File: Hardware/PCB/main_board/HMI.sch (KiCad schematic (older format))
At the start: 4 parts

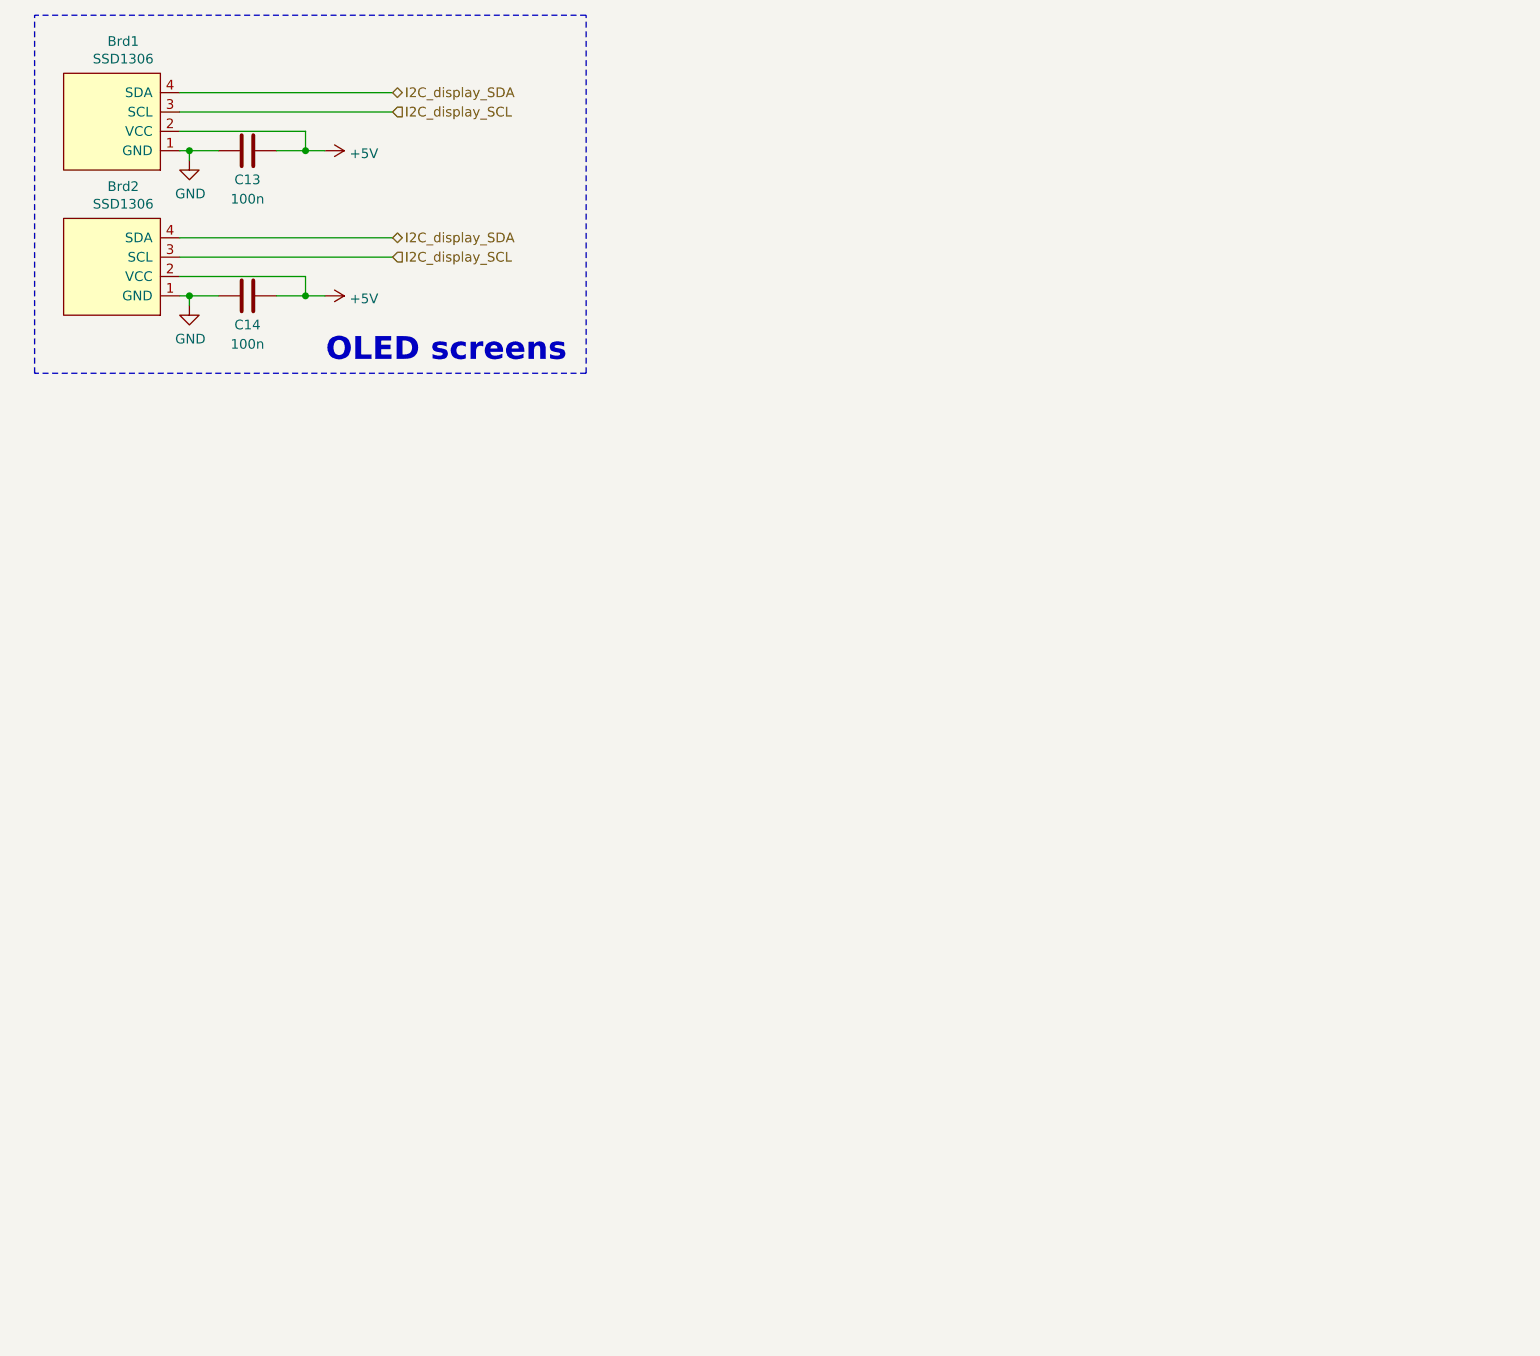
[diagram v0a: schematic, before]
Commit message: Add HMI buttons and pots to PCB
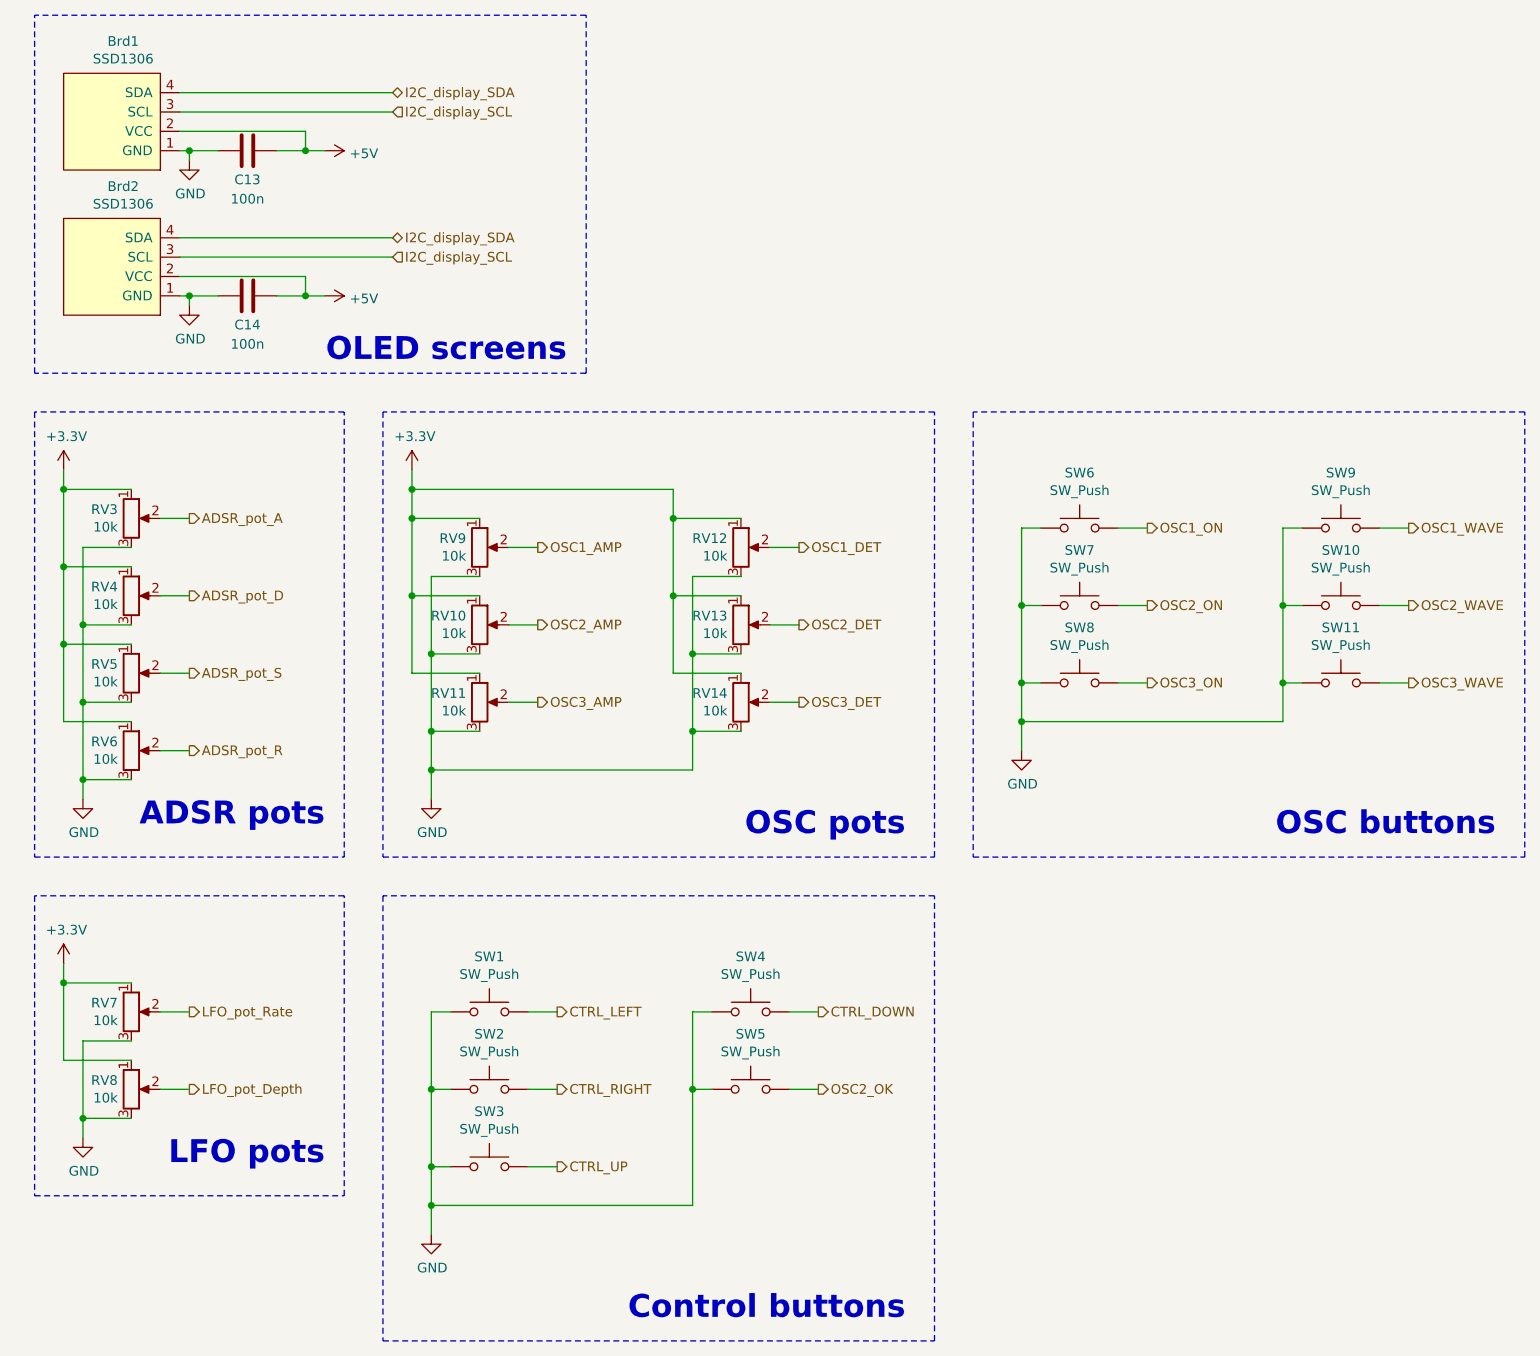
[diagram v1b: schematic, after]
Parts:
- added RV10, RV11, RV12, RV13, RV14, RV3, RV4, RV5, RV6, RV7, RV8, RV9: 10k, Potentiometer_THT:Potentiometer_Alps_RK09K_Single_Vertical, symbol Device:R_POT
- added SW1, SW10, SW11, SW2, SW3, SW4, SW5, SW6, SW7, SW8, SW9: SW_Push, Button_Switch_THT:SW_PUSH_6mm_H13mm, symbol Switch:SW_Push
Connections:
- net GND: now also RV10.3, RV11.3, RV12.3, RV13.3, RV14.3, RV3.3, RV4.3, RV5.3, RV6.3, RV7.3, RV8.3, RV9.3, SW1.1, SW10.1, SW11.1, SW2.1, SW3.1, SW4.1, SW5.1, SW6.1, SW7.1, SW8.1, SW9.1
- new net +3V3: RV10.1, RV11.1, RV12.1, RV13.1, RV14.1, RV3.1, RV4.1, RV5.1, RV6.1, RV7.1, RV8.1, RV9.1
- new net ADSR_pot_A: RV3.2
- new net ADSR_pot_D: RV4.2
- new net ADSR_pot_R: RV6.2
- new net ADSR_pot_S: RV5.2
- new net CTRL_DOWN: SW4.2
- new net CTRL_LEFT: SW1.2
- new net CTRL_RIGHT: SW2.2
- new net CTRL_UP: SW3.2
- new net LFO_pot_Depth: RV8.2
- new net LFO_pot_Rate: RV7.2
- new net OSC1_AMP: RV9.2
- new net OSC1_DET: RV12.2
- new net OSC1_ON: SW6.2
- new net OSC1_WAVE: SW9.2
- new net OSC2_AMP: RV10.2
- new net OSC2_DET: RV13.2
- new net OSC2_OK: SW5.2
- new net OSC2_ON: SW7.2
- new net OSC2_WAVE: SW10.2
- new net OSC3_AMP: RV11.2
- new net OSC3_DET: RV14.2
- new net OSC3_ON: SW8.2
- new net OSC3_WAVE: SW11.2
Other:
- note added: "ADSR pots"
- note added: "Control buttons"
- note added: "LFO pots"
- note added: "OSC buttons"
- note added: "OSC pots"

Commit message: Place HMI
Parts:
- renumbered RV3 to RV_ADSR_A1, RV4 to RV_ADSR_D1, RV6 to RV_ADSR_R1, RV5 to RV_ADSR_S1, RV8 to RV_LFO_DEPTH1, RV7 to RV_LFO_RATE1, RV9 to RV_OSC1_AMP1, RV12 to RV_OSC1_DET1, RV10 to RV_OSC2_AMP1, RV13 to RV_OSC2_DET1, RV11 to RV_OSC3_AMP1, RV14 to RV_OSC3_DET1, SW4 to SW_CTRL_DOWN1, SW1 to SW_CTRL_LEFT1, SW5 to SW_CTRL_OK1, SW2 to SW_CTRL_RIGHT1, SW3 to SW_CTRL_UP1, SW6 to SW_OSC1_ON1, SW9 to SW_OSC1_WAVE1, SW7 to SW_OSC2_ON1, SW10 to SW_OSC2_WAVE1, SW8 to SW_OSC3_ON1, SW11 to SW_OSC3_WAVE1
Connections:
- net LFO_pot_Depth renamed LFO_pot_DEPTH
- net LFO_pot_Rate renamed LFO_pot_RATE
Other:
- moved on the sheet: RV_LFO_DEPTH1, RV_LFO_RATE1, RV_OSC1_AMP1, RV_OSC1_DET1, RV_OSC2_AMP1, RV_OSC2_DET1, RV_OSC3_AMP1, RV_OSC3_DET1

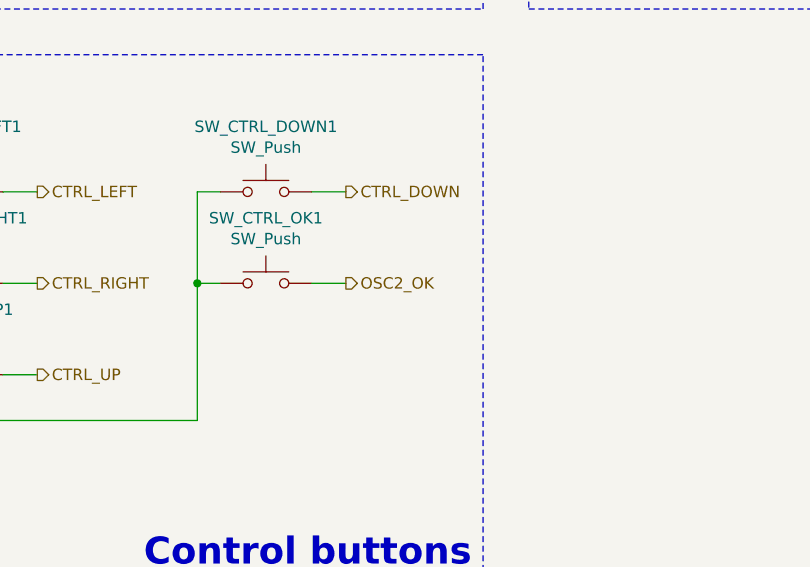
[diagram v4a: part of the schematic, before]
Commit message: Label GPIO, create HMI files
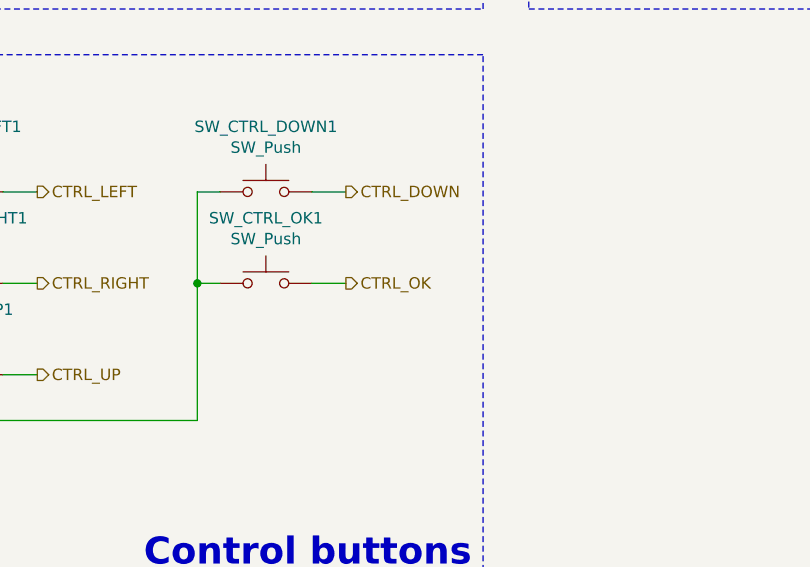
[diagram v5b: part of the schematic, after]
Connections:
- net OSC2_OK renamed CTRL_OK
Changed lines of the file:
@@
 	4600 6300 4750 6300
 Text HLabel 4750 6300 2    50   Output ~ 0
-OSC2_OK
+CTRL_OK
 Wire Wire Line
 	4200 5900 4100 5900

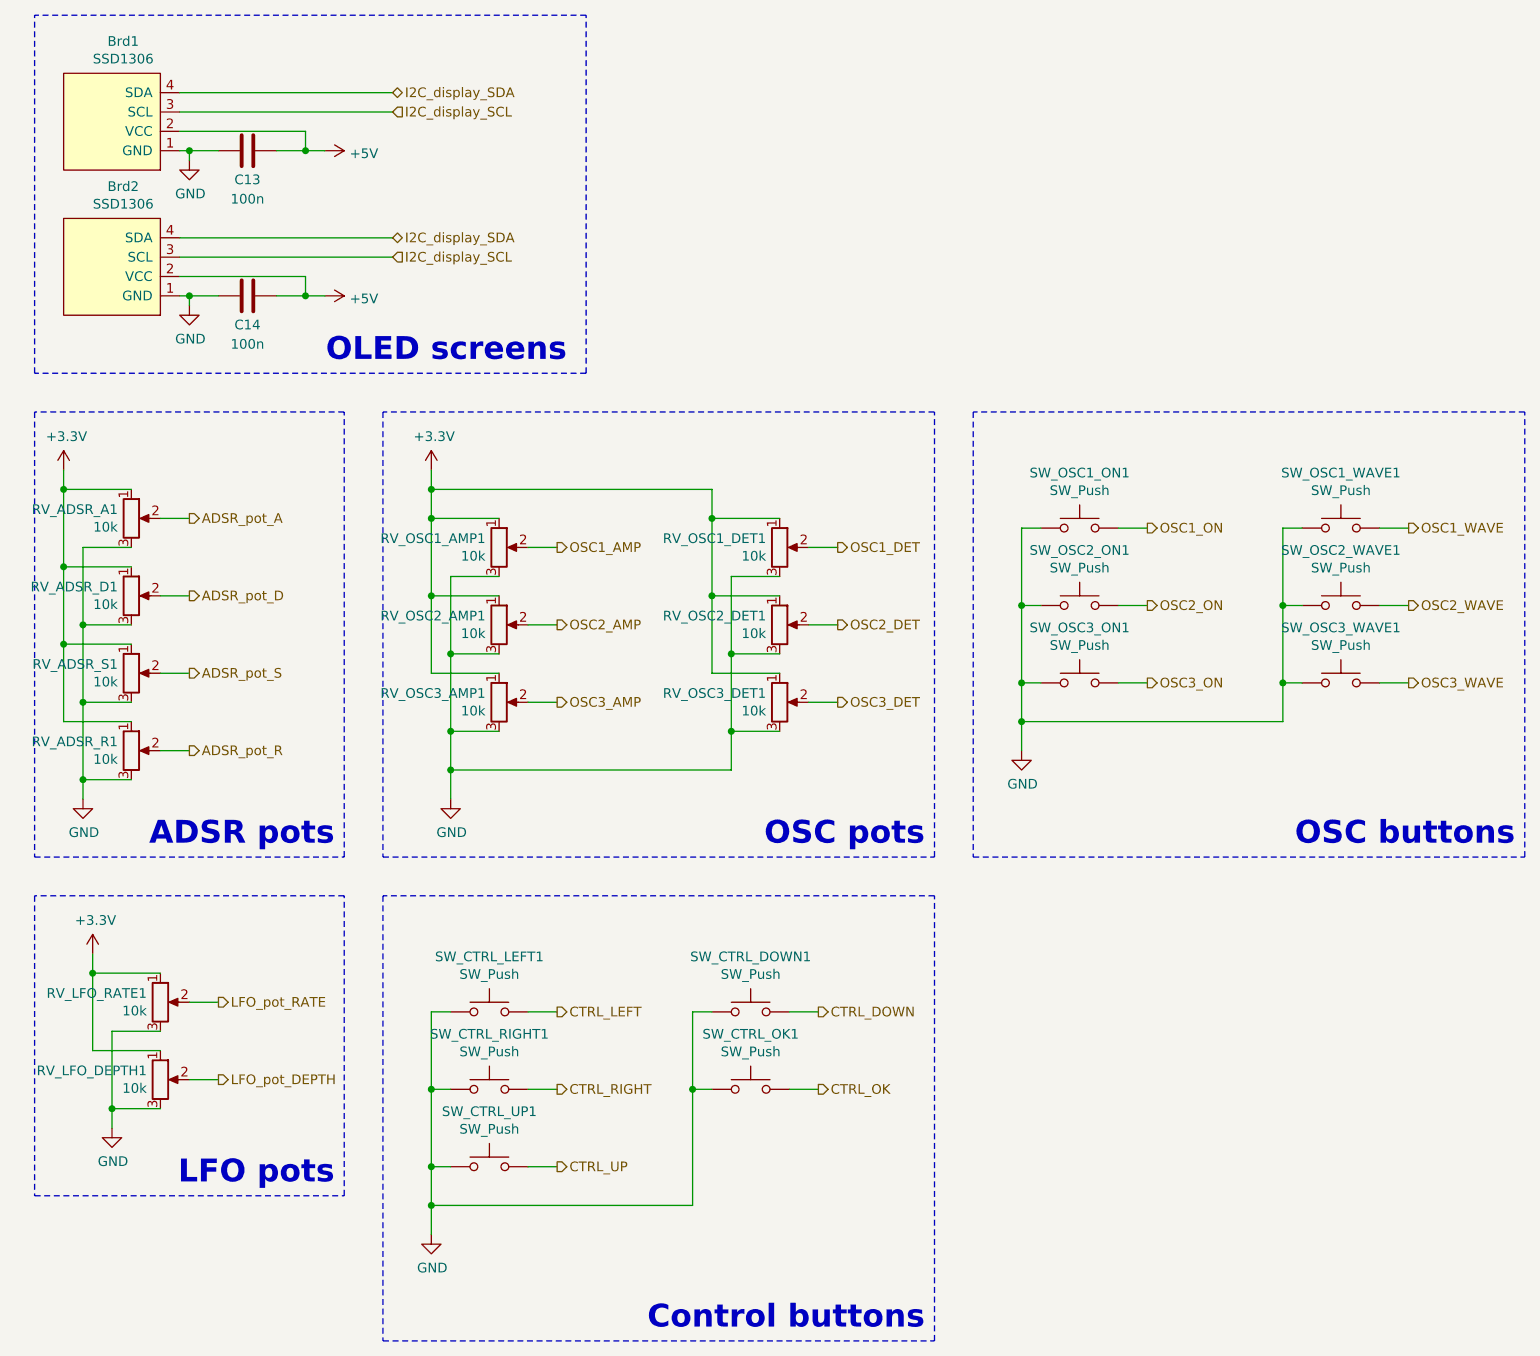
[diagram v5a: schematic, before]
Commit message: Add debounce capacitors
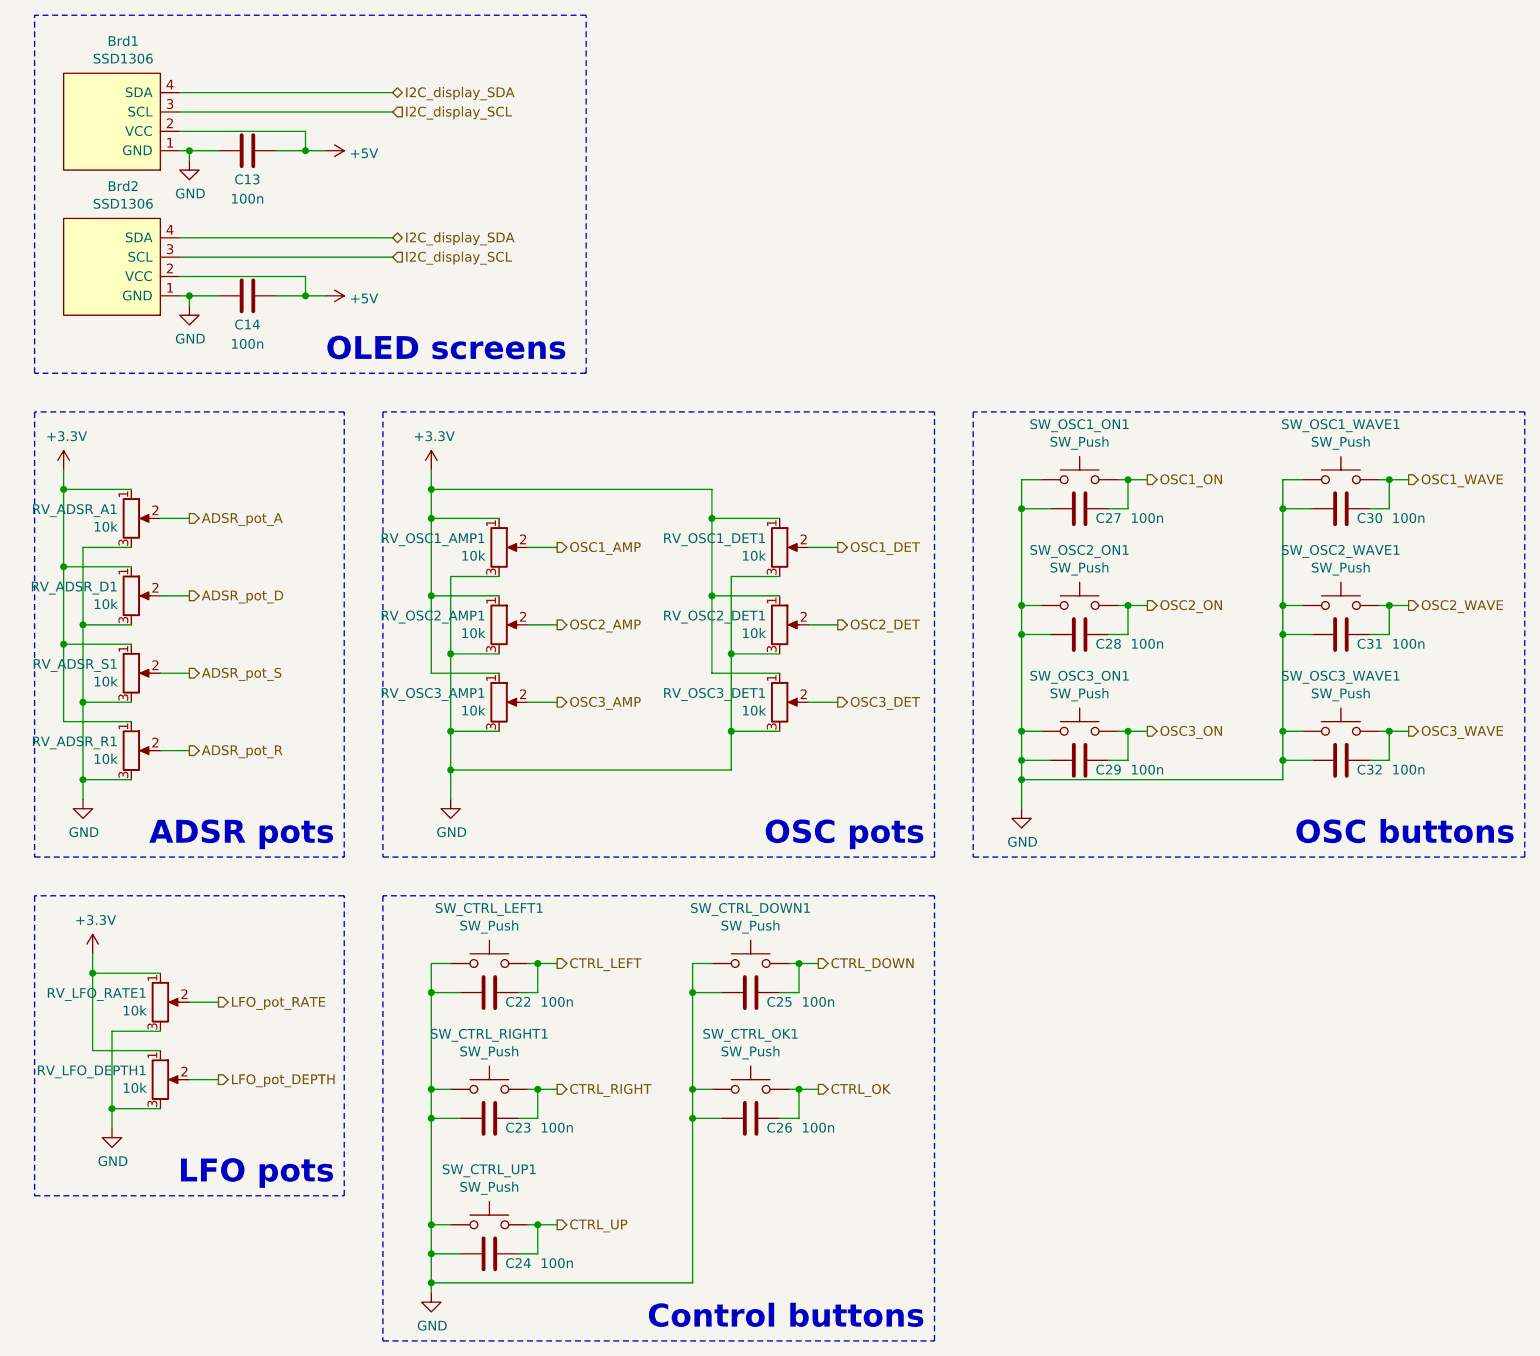
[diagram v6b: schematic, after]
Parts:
- added C22, C23, C24, C25, C26, C27, C28, C29, C30, C31, C32: 100n, Capacitor_SMD:C_0805_2012Metric, symbol Device:C
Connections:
- net CTRL_DOWN: now also C25.1
- net CTRL_LEFT: now also C22.1
- net CTRL_OK: now also C26.1
- net CTRL_RIGHT: now also C23.1
- net CTRL_UP: now also C24.1
- net GND: now also C22.2, C23.2, C24.2, C25.2, C26.2, C27.2, C28.2, C29.2, C30.2, C31.2, C32.2
- net OSC1_ON: now also C27.1
- net OSC1_WAVE: now also C30.1
- net OSC2_ON: now also C28.1
- net OSC2_WAVE: now also C31.1
- net OSC3_ON: now also C29.1
- net OSC3_WAVE: now also C32.1
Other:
- moved on the sheet: SW_CTRL_DOWN1, SW_CTRL_LEFT1, SW_CTRL_UP1, SW_OSC1_ON1, SW_OSC1_WAVE1, SW_OSC3_ON1, SW_OSC3_WAVE1
